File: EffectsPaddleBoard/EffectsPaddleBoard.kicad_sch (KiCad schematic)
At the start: 29 parts, among them J3 Barrel_Jack, U2 TPS7A0533PDBZ, U5 TPS7A0533PDBZ, U6 AP62250Z6, U8 TPS7A0518PDBZ

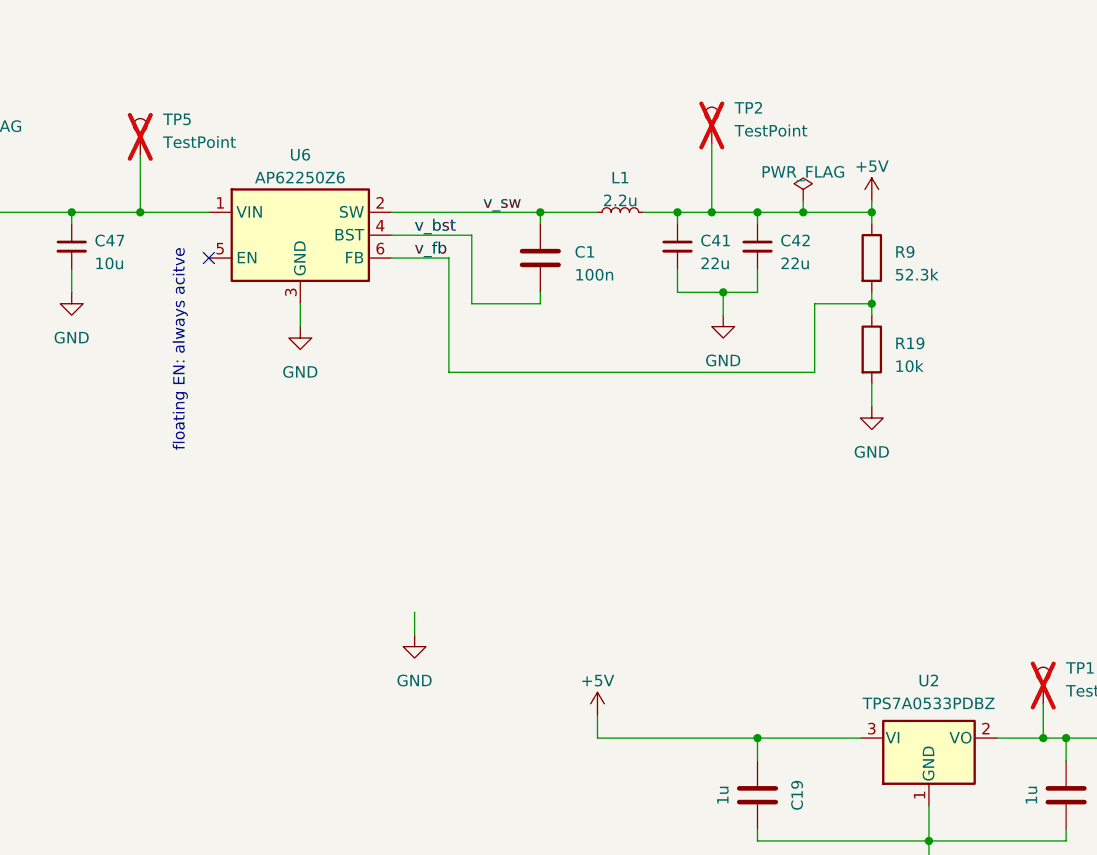
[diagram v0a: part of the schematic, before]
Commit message: Added new buck regulator, but footprint is missing
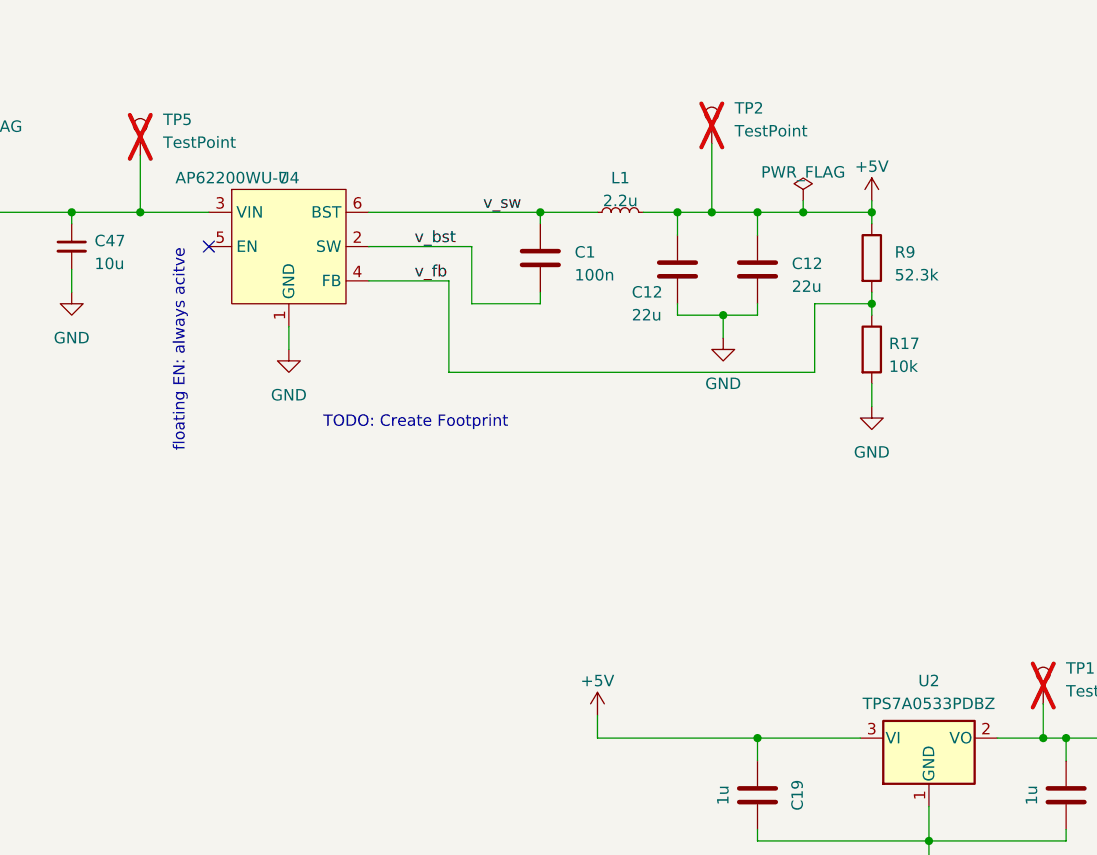
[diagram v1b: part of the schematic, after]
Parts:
- removed C41, C42: 22u, Capacitor_SMD:C_0805_2012Metric, symbol EffectsPaddleBoard:C_Small
- removed R19: 10k, Resistor_SMD:R_0402_1005Metric, symbol EffectsPaddleBoard:R
- removed U6: AP62250Z6, Package_TO_SOT_SMD:SOT-563, symbol EffectsPaddleBoard:AP62250Z6
- added C12 (x2): 22u, Capacitor_SMD:C_0805_2012Metric, symbol EffectsPaddleBoard:C
- added R17: 10k, Resistor_SMD:R_0402_1005Metric, symbol EffectsPaddleBoard:R
- added U4: AP62200WU-7, symbol EffectsPaddleBoard:AP62200WU-7
- J3: footprint Library:BarrelJack_SwitchcraftConxall_RAPC10U_Horizontal -> EffectsPaddleBoard:BarrelJack_SwitchcraftConxall_RAPC10U_Horizontal
- R9: Distributer Link https://www.mouser.ch/ProductDetail/Vishay-Beyschlag/MCS040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 -> https://www.mouser.ch/ProductDetail/Bourns/CR0402-FX-5232GL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; Manufacturer Vishay / Beyschlag -> Bourns; Manufacturer Part Number MCS04020C2200FE000 -> CR0402-FX-5232GLF
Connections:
- net +5V: now also C12.1, C12.1
- net Barreljack_in: now also U4.3 (VIN)
- net GND: now also C12.2, C12.2, R17.2, U4.1 (GND)
- net v_bst: now also U4.2 (SW)
- net v_fb: now also R17.1, U4.4 (FB)
- net v_sw: now also U4.6 (BST)
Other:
- note added: "TODO: Create Footprint"

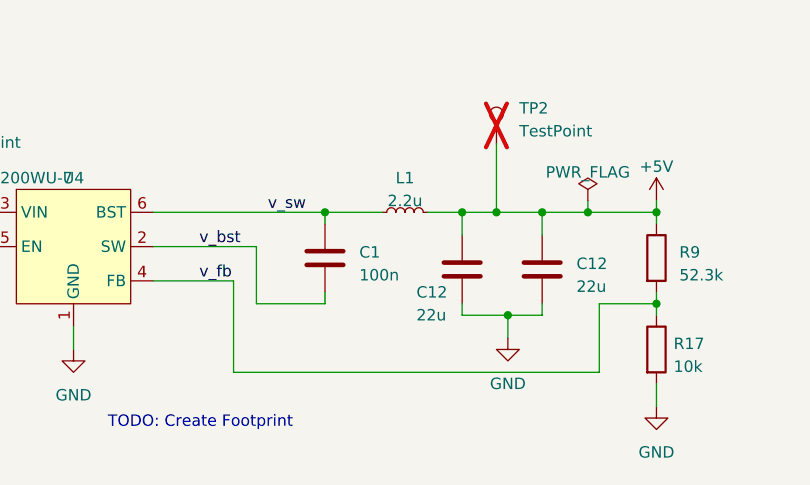
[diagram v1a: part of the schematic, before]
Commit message: Begun with double sided layout
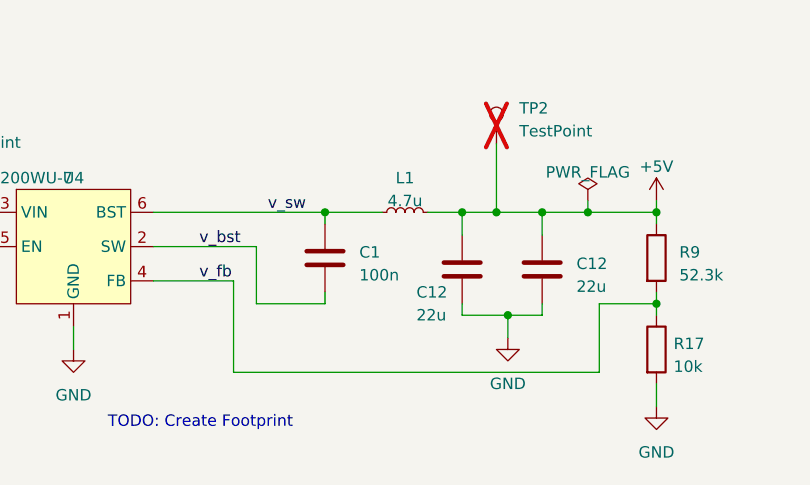
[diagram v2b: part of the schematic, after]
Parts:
- L1: value 2.2u -> 4.7u; footprint Inductor_SMD:L_1210_3225Metric -> Inductor_SMD:L_0805_2012Metric; Distributer Link https://www.bourns.com/docs/product-datasheets/srp3212.pdf -> https://www.mouser.ch/ProductDetail/Bourns/CV201210-4R7K?qs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; Manufacturer Bourns Inc. -> Bourns; Manufacturer Part Number SRP3212-2R2M -> CV201210-4R7K
- U4: footprint (none) -> EffectsPaddleBoard:TSOT26
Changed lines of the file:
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@@
       (effects (font (size 1.27 1.27)))
     )
-    (property "Footprint" "" (at 81.28 30.48 0)
+    (property "Footprint" "EffectsPaddleBoard:TSOT26" (at 81.28 30.48 0)
       (effects (font (size 1.27 1.27)) hide)
     )
@@
       (effects (font (size 1.27 1.27)))
     )
-    (property "Value" "2.2u" (at 124.46 33.02 90)
-      (effects (font (size 1.27 1.27)))
-    )
-    (property "Footprint" "Inductor_SMD:L_1210_3225Metric" (at 124.46 34.29 0)
+    (property "Value" "4.7u" (at 124.46 33.02 90)
+      (effects (font (size 1.27 1.27)))
+    )
+    (property "Footprint" "Inductor_SMD:L_0805_2012Metric" (at 124.46 34.29 0)
       (effects (font (size 1.27 1.27)) hide)
     )
@@
       (effects (font (size 1.27 1.27)) hide)
     )
-    (property "Distributer Link" "https://www.bourns.com/docs/product-datasheets/srp3212.pdf" (at 124.46 34.29 0)
-      (effects (font (size 1.27 1.27)) hide)
-    )
-    (property "Manufacturer" "Bourns Inc." (at 124.46 34.29 0)
-      (effects (font (size 1.27 1.27)) hide)
-    )
-    (property "Manufacturer Part Number" "SRP3212-2R2M" (at 124.46 34.29 0)
-      (effects (font (size 1.27 1.27)) hide)
-    )
+    (property "Distributer Link" "https://www.mouser.ch/ProductDetail/Bourns/CV201210-4R7K?qs=sGAEpiMZZMv126LJFLh8y0uVLOwDX2tIsI99wI3GnsY%3D" (at 124.46 34.29 0)
+      (effects (font (size 1.27 1.27)) hide)
+    )
+    (property "Manufacturer" "Bourns" (at 124.46 34.29 0)
+      (effects (font (size 1.27 1.27)) hide)
+    )
+    (property "Manufacturer Part Number" "CV201210-4R7K" (at 124.46 34.29 0)
+      (effects (font (size 1.27 1.27)) hide)
+    )

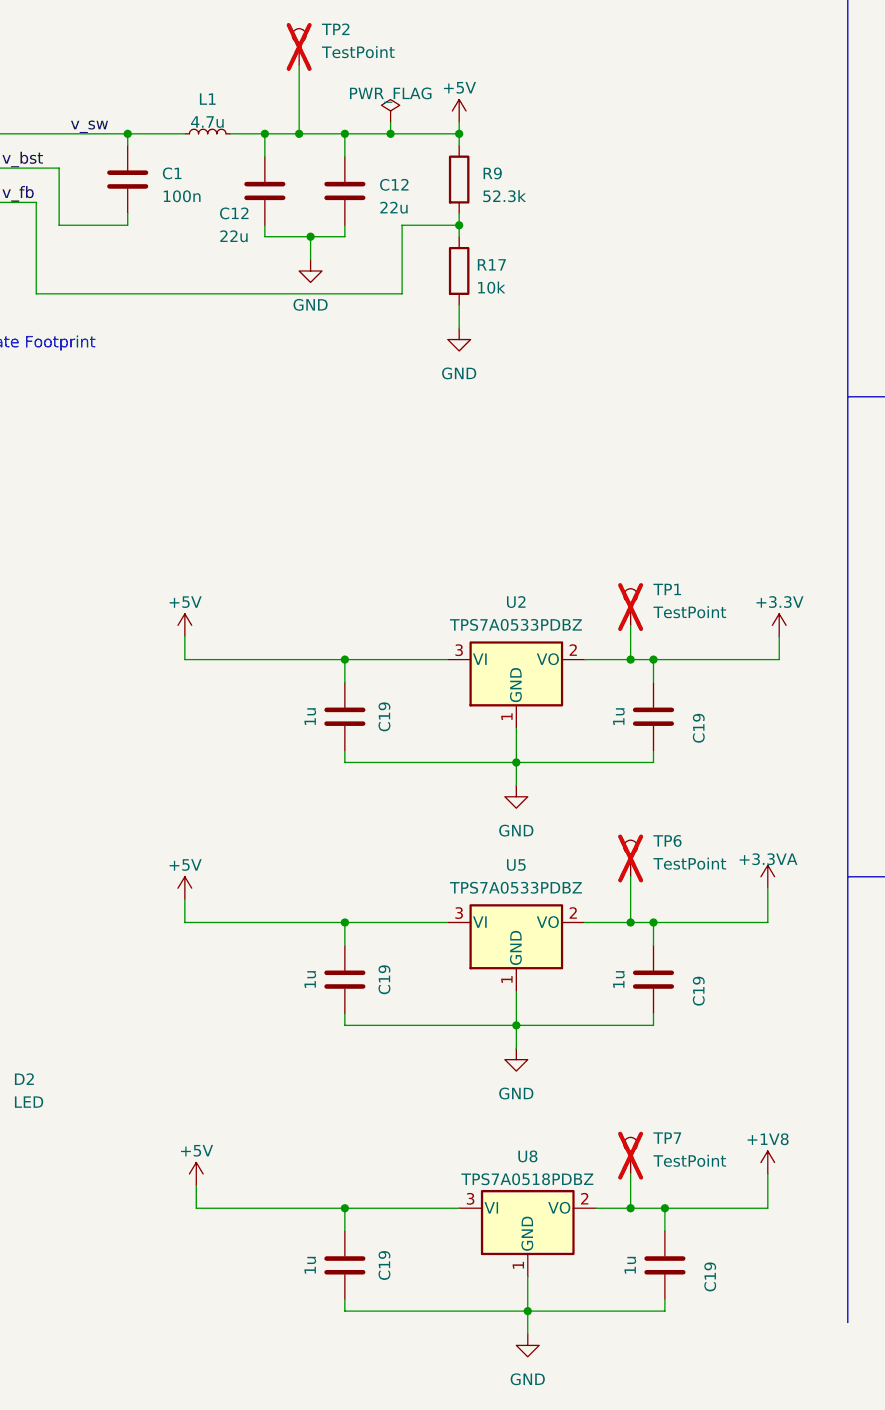
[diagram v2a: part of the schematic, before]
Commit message: Upgraded to kicad8 and improved layout
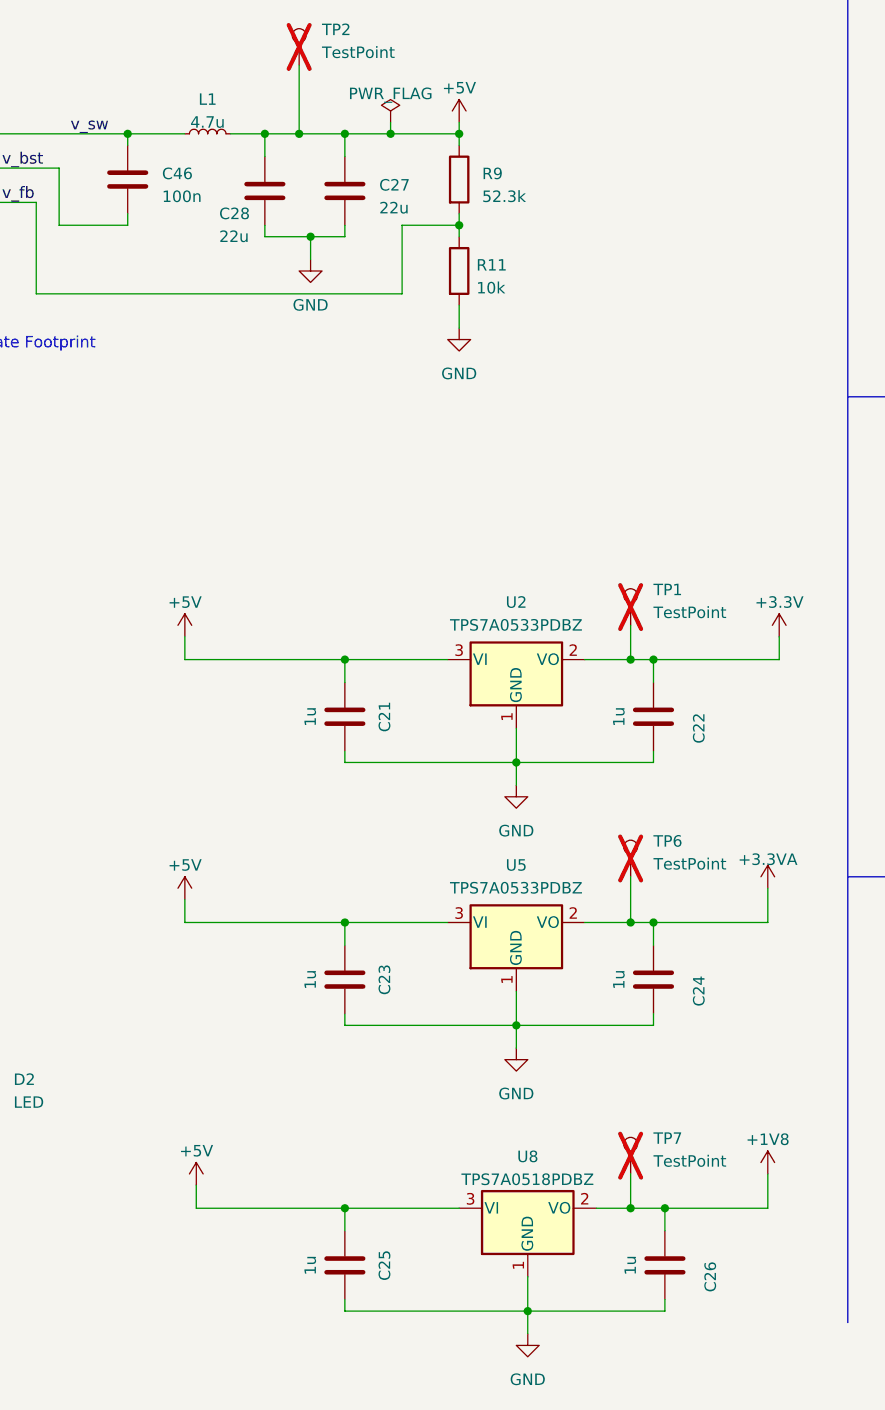
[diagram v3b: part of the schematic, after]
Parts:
- C46: renamed from C1; footprint Capacitor_SMD:C_0402_1005Metric -> Capacitor_SMD:C_0603_1608Metric
- D2, D4: footprint LED_SMD:LED_0402_1005Metric -> LED_SMD:LED_0603_1608Metric
- R11: renamed from R17; footprint Resistor_SMD:R_0402_1005Metric -> Resistor_SMD:R_0603_1608Metric
- R32, R7, R9: footprint Resistor_SMD:R_0402_1005Metric -> Resistor_SMD:R_0603_1608Metric
- renumbered C19 to C21, C19 to C22, C19 to C23, C19 to C24, C19 to C25, C19 to C26, C12 to C27, C12 to C28
